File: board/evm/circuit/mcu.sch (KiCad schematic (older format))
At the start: 1 part

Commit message: basic works for mcu
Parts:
- added C? (x8): C_104, symbol C_Small
- added C?: C_105, symbol C_Small
- added C?: C_106, symbol C_Small
- added C? (x2): C_225, symbol C_Small
- added JP?: Jumper_NO_Small, symbol Jumper_NO_Small
- added L?: Bead, symbol L_Small
- added P?: USB_OTG, symbol USB_OTG
- added P?: USB_A, symbol USB_A
- added R? (x4): R22, symbol R
- added R?: R1K, symbol R
- added R?: R10K, symbol R
- added SW?: SW_PUSH, symbol SW_PUSH
- added U?: USBLC6, symbol USBLC6
- added Y?: CRYSTAL_8M, symbol CRYSTAL_SMT
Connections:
- net labels added: +3V3, +5V, BOOT0, GND, RESET, VCC, VCC_5V
- wire segments 0 -> 83
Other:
- note added: "Reset"
- note added: "USB host\nconnect to other usb hid devices\nused for test purpose"
- note added: "USB micro connector\nconnect to host instead of wireless link\ncharge battery\n"
- moved on the sheet: U?

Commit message: add more schs
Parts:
- added IC?: AT24CS64-SSHM, SO8, symbol AT24CS64-SSHM
- added R? (x2): R10K, symbol R
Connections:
- net labels added: A16, A17, A18, A19, A20, A21, A22, A23, D0, D1, D10, D11, D12, D13, D14, D15, D2, D3, D4, D5, D6, D7, D8, D9, EEPROM_SCL, EEPROM_SDA, nCS, nOE, nWE
- wire segments 83 -> 133

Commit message: working on leak current detection
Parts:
- removed P?: USB_OTG, symbol USB_OTG
- removed P?: USB_A, symbol USB_A
- removed U?: USBLC6, symbol USBLC6
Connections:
- net labels added: Device_D+, Device_D-, Host_D+, Host_D-
- net labels removed: +5V, VCC_5V
- wire segments 133 -> 62
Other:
- note removed: "USB host\nconnect to other usb hid devices\nused for test purpose"
- note removed: "USB micro connector\nconnect to host instead of wireless link\ncharge battery\n"

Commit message: evm sch design finished
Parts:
- removed IC?: AT24CS64-SSHM, SO8, symbol AT24CS64-SSHM
- removed R? (x2): R10K, symbol R
- added D?: LED, symbol LED
- added J?: TagConnect, symbol TagConnect
- added R?: R10K, symbol R
- added R?: R1K, symbol R
- added U?: W25Q32, symbol W25Q
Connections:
- net labels added: FLASH_CLK, FLASH_SI, FLASH_SO, FLASH_nCS, GPIO0, GPIO1, GPIO10, GPIO2, GPIO3, GPIO4, GPIO5, GPIO6, GPIO7, GPIO8, GPIO9, I2C1_SCL, I2C1_SDA, I2C2_SCL, I2C2_SDA, I2C3_SCL, I2C3_SDA, I2C4_SCL, I2C4_SDA, IRQ0, IRQ1, IRQ2, IRQ3, SPI2_MISO, SPI2_MOSI, SPI2_NSS, SPI2_SCK, SPI3_MISO, SPI3_MOSI, SPI3_NSS, SPI3_SCK, SWCLK, SWDIO
- net labels removed: EEPROM_SCL, EEPROM_SDA
- wire segments 62 -> 88
- no-connect marks 0 -> 10
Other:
- moved on the sheet: R?

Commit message: add light sensor
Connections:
- net labels added: ADC_IN
- wire segments 88 -> 118
- no-connect marks 10 -> 9
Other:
- moved on the sheet: D?, R?
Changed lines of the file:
@@
 $EndComp
 Wire Wire Line
-	8000 2300 8000 3100
+	8000 2300 8000 2450
+Wire Wire Line
+	8000 2450 8000 2800
+Wire Wire Line
+	8000 2800 8000 3100
 Connection ~ 8000 3100
 Connection ~ 8100 3100
@@
 	8100 9000 8100 9150
 Wire Wire Line
-	8100 9000 8500 9000
+	8100 9000 8200 9000
+Wire Wire Line
+	8200 9000 8300 9000
+Wire Wire Line
+	8300 9000 8400 9000
+Wire Wire Line
+	8400 9000 8500 9000
 Connection ~ 8100 9000
 Connection ~ 8200 9000
@@
 $EndComp
 Wire Wire Line
-	8000 2450 10500 2450
+	8000 2450 8400 2450
+Wire Wire Line
+	8400 2450 8700 2450
+Wire Wire Line
+	8700 2450 9000 2450
+Wire Wire Line
+	9000 2450 9300 2450
+Wire Wire Line
+	9300 2450 9600 2450
+Wire Wire Line
+	9600 2450 9900 2450
+Wire Wire Line
+	9900 2450 10200 2450
+Wire Wire Line
+	10200 2450 10500 2450
 Connection ~ 8000 2450
 Connection ~ 8400 2450
@@
 Connection ~ 10200 2450
 Wire Wire Line
-	8400 2650 10500 2650
+	8400 2650 8700 2650
+Wire Wire Line
+	8700 2650 9000 2650
+Wire Wire Line
+	9000 2650 9300 2650
+Wire Wire Line
+	9300 2650 9600 2650
+Wire Wire Line
+	9600 2650 9900 2650
+Wire Wire Line
+	9900 2650 10200 2650
+Wire Wire Line
+	10200 2650 10500 2650
 Connection ~ 8700 2650
 Connection ~ 9000 2650
@@
 	1550 3200 1550 3150
 Wire Wire Line
-	1550 3500 1550 3750
+	1550 3500 1550 3600
+Wire Wire Line
+	1550 3600 1550 3750
 Wire Wire Line
 	2150 3600 3800 3600
@@
 $EndComp
 Wire Wire Line
-	2750 3250 2750 4000
-Wire Wire Line
-	2750 4000 3800 4000
+	2750 3250 2750 3800
+Wire Wire Line
+	2750 3800 2750 4000
+Wire Wire Line
+	2750 4000 3600 4000
+Wire Wire Line
+	3600 4000 3800 4000
 Wire Wire Line
 	3600 4100 3800 4100
@@
 $EndComp
 Wire Wire Line
-	8000 3100 8500 3100
+	8000 3100 8100 3100
+Wire Wire Line
+	8100 3100 8200 3100
+Wire Wire Line
+	8200 3100 8300 3100
+Wire Wire Line
+	8300 3100 8400 3100
+Wire Wire Line
+	8400 3100 8500 3100
 $Comp
 L L_Small L?
@@
 	8600 3100 8600 3000
 Wire Wire Line
-	8000 2800 8800 2800
+	8000 2800 8600 2800
+Wire Wire Line
+	8600 2800 8800 2800
 Connection ~ 8000 2800
 $Comp
@@
 	3650 4300 3800 4300
 Wire Wire Line
-	3350 4500 3350 4650
+	3350 4500 3350 4600
+Wire Wire Line
+	3350 4600 3350 4650
 Wire Wire Line
 	3650 4500 3650 4600
@@
 	3150 3800 3800 3800
 Wire Wire Line
-	2600 3800 2850 3800
+	2600 3800 2750 3800
+Wire Wire Line
+	2750 3800 2850 3800
 Connection ~ 2750 3800
 $Comp
@@
 	14800 3050 14700 3050
 Wire Wire Line
-	14800 2750 14800 3150
+	14800 2750 14800 2850
+Wire Wire Line
+	14800 2850 14800 3050
+Wire Wire Line
+	14800 3050 14800 3150
 $Comp
 L GND #PWR?
@@
 L LED D?
 U 1 1 578831CF
-P 13200 8500
-F 0 "D?" H 13200 8600 50  0000 C CNN
-F 1 "LED" H 13200 8400 50  0000 C CNN
-F 2 "" H 13200 8500 50  0000 C CNN
-F 3 "" H 13200 8500 50  0000 C CNN
-	1    13200 8500
+P 13500 8400
+F 0 "D?" H 13500 8500 50  0000 C CNN
+F 1 "LED" H 13500 8300 50  0000 C CNN
+F 2 "" H 13500 8400 50  0000 C CNN
+F 3 "" H 13500 8400 50  0000 C CNN
+	1    13500 8400
 	1    0    0    -1
 $EndComp
@@
 L +3V3 #PWR?
 U 1 1 578832F8
-P 14100 8350
-F 0 "#PWR?" H 14100 8200 50  0001 C CNN
-F 1 "+3V3" H 14100 8490 50  0000 C CNN
-F 2 "" H 14100 8350 50  0000 C CNN
-F 3 "" H 14100 8350 50  0000 C CNN
-	1    14100 8350
+P 14100 8250
+F 0 "#PWR?" H 14100 8100 50  0001 C CNN
+F 1 "+3V3" H 14100 8390 50  0000 C CNN
+F 2 "" H 14100 8250 50  0000 C CNN
+F 3 "" H 14100 8250 50  0000 C CNN
+	1    14100 8250
 	1    0    0    -1
 $EndComp
@@
 L R R?
 U 1 1 57883381
-P 13750 8500
-F 0 "R?" V 13830 8500 50  0000 C CNN
-F 1 "R1K" V 13750 8500 50  0000 C CNN
-F 2 "" V 13680 8500 50  0000 C CNN
-F 3 "" H 13750 8500 50  0000 C CNN
-	1    13750 8500
+P 13900 8400
+F 0 "R?" V 13980 8400 50  0000 C CNN
+F 1 "R1K" V 13900 8400 50  0000 C CNN
+F 2 "" V 13830 8400 50  0000 C CNN
+F 3 "" H 13900 8400 50  0000 C CNN
+	1    13900 8400
 	0    1    1    0
 $EndComp
 Wire Wire Line
-	13900 8500 14100 8500
-Wire Wire Line
-	14100 8500 14100 8350
-Wire Wire Line
-	13600 8500 13400 8500
-Wire Wire Line
-	13000 8500 12800 8500
+	14050 8400 14100 8400
+Wire Wire Line
+	14100 8400 14100 8250
+Wire Wire Line
+	13750 8400 13700 8400
+Wire Wire Line
+	13300 8400 12800 8400
 NoConn ~ 12800 6500
 NoConn ~ 12800 6100
 NoConn ~ 12800 7800
 NoConn ~ 12800 8300
-NoConn ~ 12800 8400
 NoConn ~ 3800 5300
 NoConn ~ 3800 5400
 NoConn ~ 3800 7300
 NoConn ~ 3800 7200
+Text HLabel 12800 8500 2    60   Input ~ 0
+ADC_IN
 $EndSCHEMATC

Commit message: bug fix
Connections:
- wire segments 118 -> 89
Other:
- moved on the sheet: JP?
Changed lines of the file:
@@
 LIBS:Altera
 LIBS:my_kicad
+LIBS:Oscillators
 LIBS:oh-my-keyboard-cache
 EELAYER 25 0
@@
 $EndComp
 Wire Wire Line
-	8000 2300 8000 2450
-Wire Wire Line
-	8000 2450 8000 2800
-Wire Wire Line
-	8000 2800 8000 3100
+	8000 2300 8000 3100
 Connection ~ 8000 3100
 Connection ~ 8100 3100
@@
 	8100 9000 8100 9150
 Wire Wire Line
-	8100 9000 8200 9000
-Wire Wire Line
-	8200 9000 8300 9000
-Wire Wire Line
-	8300 9000 8400 9000
-Wire Wire Line
-	8400 9000 8500 9000
+	8100 9000 8500 9000
 Connection ~ 8100 9000
 Connection ~ 8200 9000
@@
 $EndComp
 Wire Wire Line
-	8000 2450 8400 2450
-Wire Wire Line
-	8400 2450 8700 2450
-Wire Wire Line
-	8700 2450 9000 2450
-Wire Wire Line
-	9000 2450 9300 2450
-Wire Wire Line
-	9300 2450 9600 2450
-Wire Wire Line
-	9600 2450 9900 2450
-Wire Wire Line
-	9900 2450 10200 2450
-Wire Wire Line
-	10200 2450 10500 2450
+	8000 2450 10500 2450
 Connection ~ 8000 2450
 Connection ~ 8400 2450
@@
 Connection ~ 10200 2450
 Wire Wire Line
-	8400 2650 8700 2650
-Wire Wire Line
-	8700 2650 9000 2650
-Wire Wire Line
-	9000 2650 9300 2650
-Wire Wire Line
-	9300 2650 9600 2650
-Wire Wire Line
-	9600 2650 9900 2650
-Wire Wire Line
-	9900 2650 10200 2650
-Wire Wire Line
-	10200 2650 10500 2650
+	8400 2650 10500 2650
 Connection ~ 8700 2650
 Connection ~ 9000 2650
@@
 	1550 3200 1550 3150
 Wire Wire Line
-	1550 3500 1550 3600
-Wire Wire Line
-	1550 3600 1550 3750
+	1550 3500 1550 3750
 Wire Wire Line
 	2150 3600 3800 3600
@@
 $EndComp
 Wire Wire Line
-	2750 3250 2750 3800
-Wire Wire Line
-	2750 3800 2750 4000
-Wire Wire Line
-	2750 4000 3600 4000
-Wire Wire Line
-	3600 4000 3800 4000
-Wire Wire Line
-	3600 4100 3800 4100
-Wire Wire Line
-	3600 4100 3600 4000
-Connection ~ 3600 4000
+	2750 4100 3800 4100
 $Comp
 L GND #PWR?
@@
 $EndComp
 Wire Wire Line
-	8000 3100 8100 3100
-Wire Wire Line
-	8100 3100 8200 3100
-Wire Wire Line
-	8200 3100 8300 3100
-Wire Wire Line
-	8300 3100 8400 3100
-Wire Wire Line
-	8400 3100 8500 3100
+	8000 3100 8500 3100
 $Comp
 L L_Small L?
@@
 	8600 3100 8600 3000
 Wire Wire Line
-	8000 2800 8600 2800
-Wire Wire Line
-	8600 2800 8800 2800
+	8000 2800 8800 2800
 Connection ~ 8000 2800
 $Comp
@@
 	3650 4300 3800 4300
 Wire Wire Line
-	3350 4500 3350 4600
-Wire Wire Line
-	3350 4600 3350 4650
+	3350 4500 3350 4650
 Wire Wire Line
 	3650 4500 3650 4600
@@
 	0    -1   -1   0
 $EndComp
-Wire Wire Line
-	3150 3800 3800 3800
-Wire Wire Line
-	2600 3800 2750 3800
-Wire Wire Line
-	2750 3800 2850 3800
-Connection ~ 2750 3800
 $Comp
 L Jumper_NO_Small JP?
 U 1 1 5756C9A0
-P 2500 3800
-F 0 "JP?" H 2500 3880 50  0000 C CNN
-F 1 "Jumper_NO_Small" H 2510 3740 50  0001 C CNN
-F 2 "" H 2500 3800 50  0000 C CNN
-F 3 "" H 2500 3800 50  0000 C CNN
-	1    2500 3800
-	1    0    0    -1
+P 3250 3950
+F 0 "JP?" H 3250 4030 50  0000 C CNN
+F 1 "Jumper_NO_Small" H 3260 3890 50  0001 C CNN
+F 2 "" H 3250 3950 50  0000 C CNN
+F 3 "" H 3250 3950 50  0000 C CNN
+	1    3250 3950
+	-1   0    0    1
 $EndComp
 $Comp
 L GND #PWR?
 U 1 1 5756CAC3
-P 2300 3950
-F 0 "#PWR?" H 2300 3700 50  0001 C CNN
-F 1 "GND" H 2300 3800 50  0000 C CNN
-F 2 "" H 2300 3950 50  0000 C CNN
-F 3 "" H 2300 3950 50  0000 C CNN
-	1    2300 3950
-	1    0    0    -1
-$EndComp
-Wire Wire Line
-	2300 3950 2300 3800
-Wire Wire Line
-	2300 3800 2400 3800
+P 3100 4000
+F 0 "#PWR?" H 3100 3750 50  0001 C CNN
+F 1 "GND" H 3100 3850 50  0000 C CNN
+F 2 "" H 3100 4000 50  0000 C CNN
+F 3 "" H 3100 4000 50  0000 C CNN
+	1    3100 4000
+	1    0    0    -1
+$EndComp
 $Comp
 L R R?
@@
 	14800 3050 14700 3050
 Wire Wire Line
-	14800 2750 14800 2850
-Wire Wire Line
-	14800 2850 14800 3050
-Wire Wire Line
-	14800 3050 14800 3150
+	14800 2750 14800 3150
 $Comp
 L GND #PWR?
@@
 Text HLabel 12800 8500 2    60   Input ~ 0
 ADC_IN
+Wire Wire Line
+	3800 4000 3700 4000
+Wire Wire Line
+	3700 4000 3700 4100
+Connection ~ 3700 4100
+Wire Wire Line
+	3150 3800 3800 3800
+Wire Wire Line
+	2850 3800 2750 3800
+Wire Wire Line
+	2750 3250 2750 4100
+Connection ~ 2750 3800
+Wire Wire Line
+	3350 3950 3350 3800
+Connection ~ 3350 3800
+Wire Wire Line
+	3100 4000 3100 3950
+Wire Wire Line
+	3100 3950 3150 3950
 $EndSCHEMATC

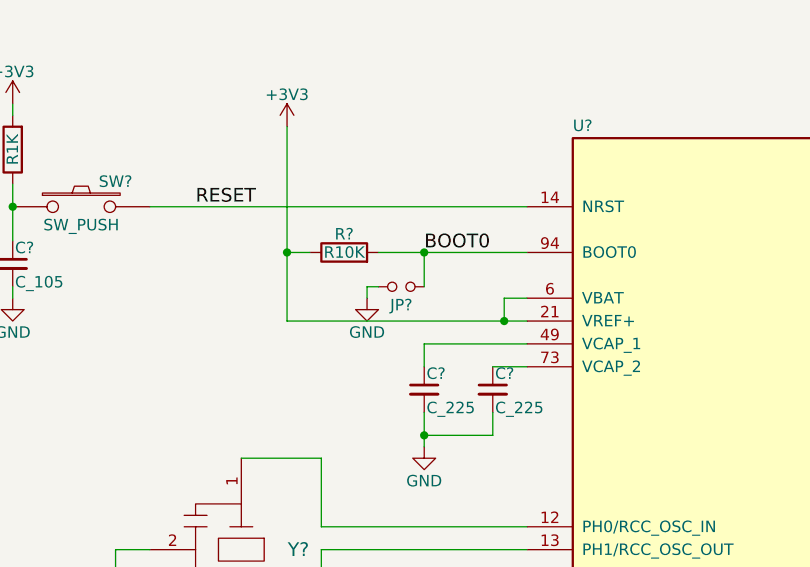
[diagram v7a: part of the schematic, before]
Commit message: set boot0 to 0
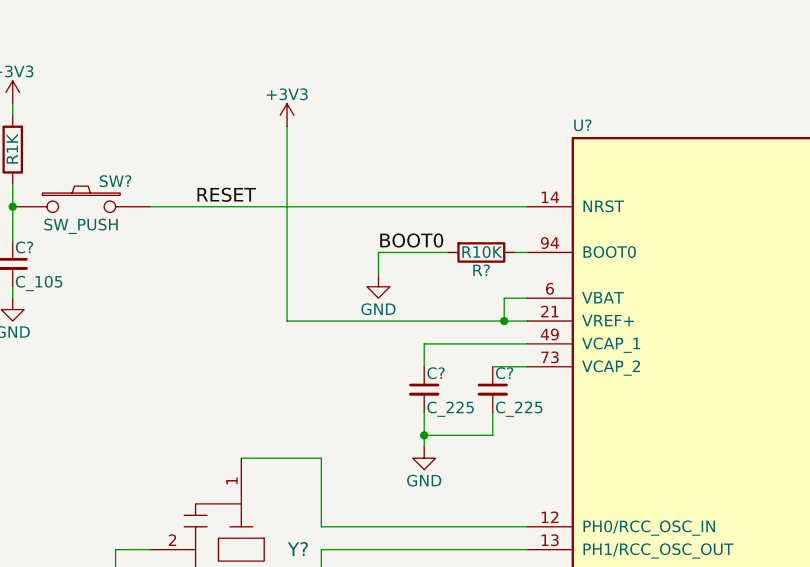
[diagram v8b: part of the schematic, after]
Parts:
- removed JP?: Jumper_NO_Small, symbol Jumper_NO_Small
- removed R?: R10K, symbol R
- added R?: R10K, symbol R
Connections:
- wire segments 89 -> 87
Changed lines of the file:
@@
 Connection ~ 3350 4600
-$Comp
-L R R?
-U 1 1 5756C793
-P 3000 3800
-F 0 "R?" V 3080 3800 50  0000 C CNN
-F 1 "R10K" V 3000 3800 50  0000 C CNN
-F 2 "" V 2930 3800 50  0000 C CNN
-F 3 "" H 3000 3800 50  0000 C CNN
-	1    3000 3800
-	0    -1   -1   0
-$EndComp
-$Comp
-L Jumper_NO_Small JP?
-U 1 1 5756C9A0
-P 3250 3950
-F 0 "JP?" H 3250 4030 50  0000 C CNN
-F 1 "Jumper_NO_Small" H 3260 3890 50  0001 C CNN
-F 2 "" H 3250 3950 50  0000 C CNN
-F 3 "" H 3250 3950 50  0000 C CNN
-	1    3250 3950
-	-1   0    0    1
-$EndComp
 $Comp
 L GND #PWR?
 U 1 1 5756CAC3
-P 3100 4000
-F 0 "#PWR?" H 3100 3750 50  0001 C CNN
-F 1 "GND" H 3100 3850 50  0000 C CNN
-F 2 "" H 3100 4000 50  0000 C CNN
-F 3 "" H 3100 4000 50  0000 C CNN
-	1    3100 4000
+P 3150 3900
+F 0 "#PWR?" H 3150 3650 50  0001 C CNN
+F 1 "GND" H 3150 3750 50  0000 C CNN
+F 2 "" H 3150 3900 50  0000 C CNN
+F 3 "" H 3150 3900 50  0000 C CNN
+	1    3150 3900
 	1    0    0    -1
 $EndComp
@@
 Text Label 2350 3600 0    60   ~ 0
 RESET
-Text Label 3350 3800 0    60   ~ 0
+Text Label 3150 3800 0    60   ~ 0
 BOOT0
 $Comp
@@
 Connection ~ 3700 4100
 Wire Wire Line
-	3150 3800 3800 3800
-Wire Wire Line
-	2850 3800 2750 3800
-Wire Wire Line
 	2750 3250 2750 4100
-Connection ~ 2750 3800
-Wire Wire Line
-	3350 3950 3350 3800
-Connection ~ 3350 3800
-Wire Wire Line
-	3100 4000 3100 3950
-Wire Wire Line
-	3100 3950 3150 3950
+Wire Wire Line
+	3150 3800 3150 3900
+Wire Wire Line
+	3450 3800 3150 3800
+$Comp
+L R R?
+U 1 1 575DEFBD
+P 3600 3800
+F 0 "R?" V 3680 3800 50  0000 C CNN
+F 1 "R10K" V 3600 3800 50  0000 C CNN
+F 2 "" V 3530 3800 50  0000 C CNN
+F 3 "" H 3600 3800 50  0000 C CNN
+	1    3600 3800
+	0    1    1    0
+$EndComp
+Wire Wire Line
+	3750 3800 3800 3800
 $EndSCHEMATC
